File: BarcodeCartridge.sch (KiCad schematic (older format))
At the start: 3 parts, among them J1 Cartridge Connector, U1 W25Q128

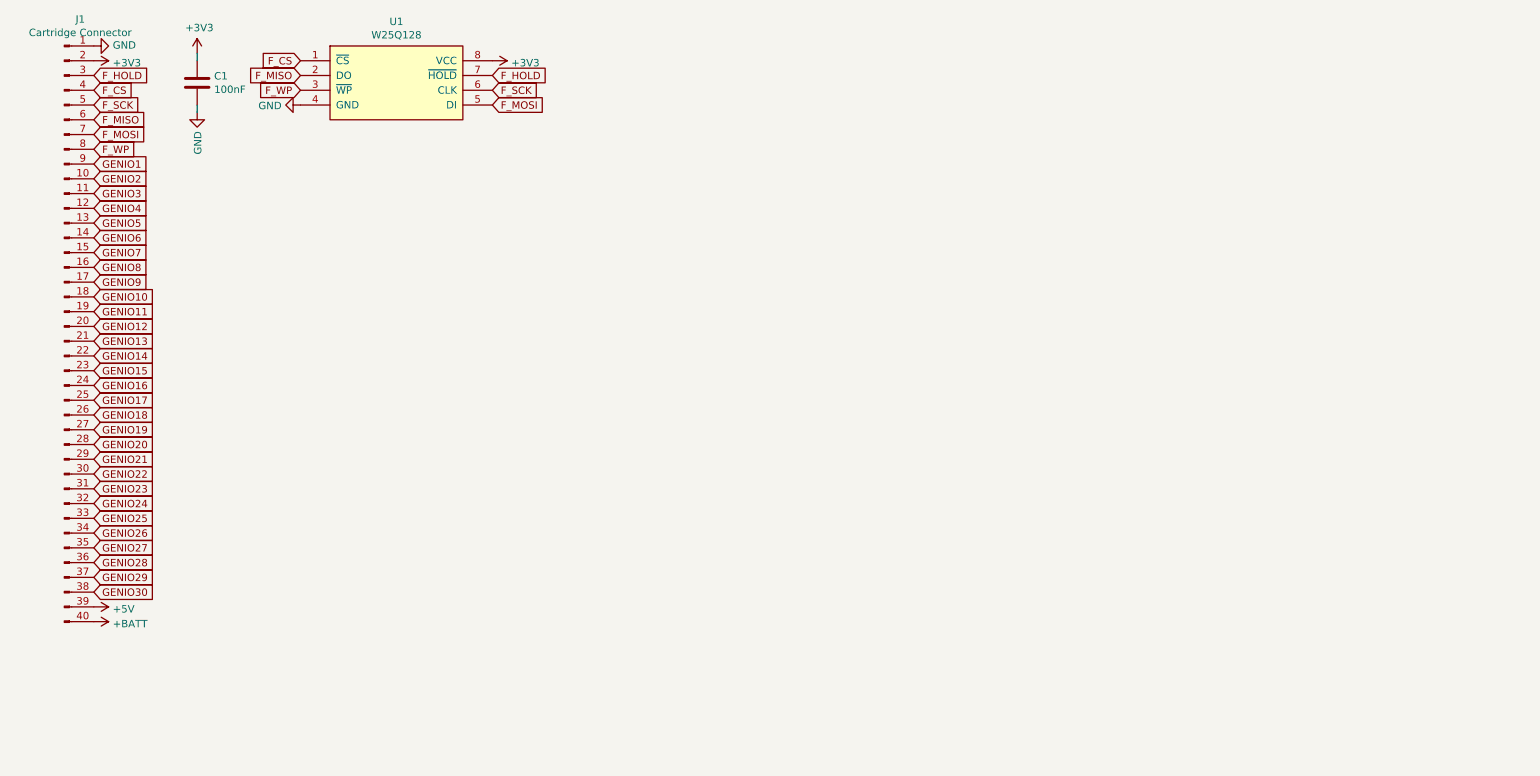
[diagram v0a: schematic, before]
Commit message: First design of the Barcode reader cartridge
Also updated:
- README
- Render image
- .gitignore
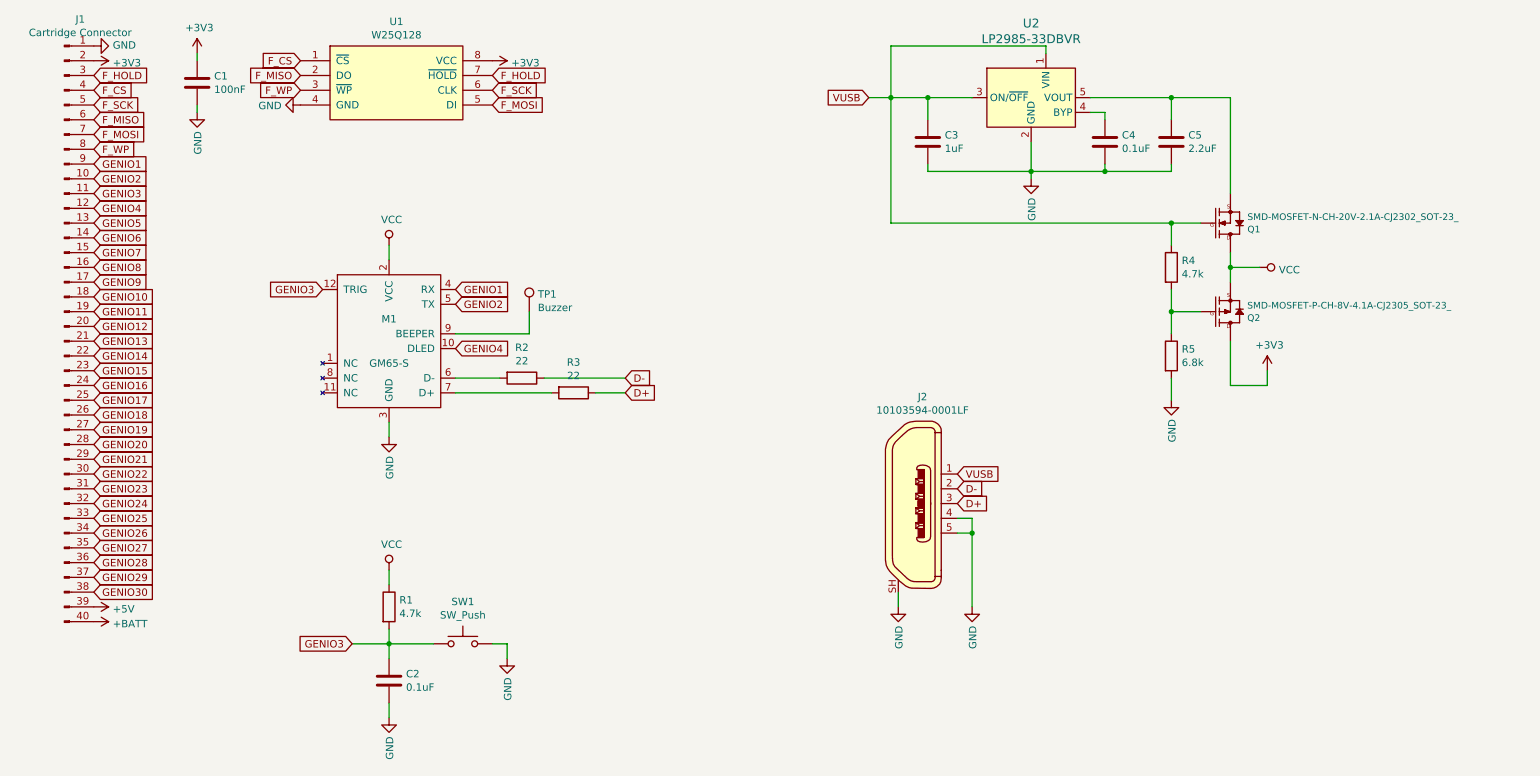
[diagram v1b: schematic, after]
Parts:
- added C2, C4: 0.1uF, Capacitors_SMD:C_0805_HandSoldering, symbol device:C
- added C3: 1uF, Capacitors_SMD:C_0805_HandSoldering, symbol device:C
- added C5: 2.2uF, Capacitors_SMD:C_0805_HandSoldering, symbol device:C
- added J2: 10103594-0001LF, digikey-footprints:USB_Micro_B_Female_10103594-0001LF, symbol dk_USB-DVI-HDMI-Connectors:10103594-0001LF
- added M1: GM65-S, SuperconCartridge:SD-52892-044, symbol SuperconCartridge:GM65-S
- added Q1: SMD-MOSFET-N-CH-20V-2.1A-CJ2302_SOT-23_, TO_SOT_Packages_SMD:SOT-23, symbol SeeedOPL-Transistor-2016:SMD-MOSFET-N-CH-20V-2.1A-CJ2302_SOT-23_
- added Q2: SMD-MOSFET-P-CH-8V-4.1A-CJ2305_SOT-23_, TO_SOT_Packages_SMD:SOT-23, symbol SeeedOPL-Transistor-2016:SMD-MOSFET-P-CH-8V-4.1A-CJ2305_SOT-23_
- added R1, R4: 4.7k, Resistors_SMD:R_0805_HandSoldering, symbol device:R
- added R2, R3: 22, Resistors_SMD:R_0805_HandSoldering, symbol device:R
- added R5: 6.8k, Resistors_SMD:R_0805_HandSoldering, symbol device:R
- added SW1: SW_Push, Buttons_Switches_SMD:SW_SPST_PTS645, symbol Switch:SW_Push
- added TP1: Buzzer, Connectors_TestPoints:Test_Point_Pad_d2.0mm, symbol Connector:TestPoint
- added U2: LP2985-33DBVR, digikey-footprints:SOT-753, symbol dk_PMIC-Voltage-Regulators-Linear:LP2985-33DBVR
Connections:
- net +3V3: now also Q2.3 (D)
- net GENIO1: now also M1.4 (RX)
- net GENIO2: now also M1.5 (TX)
- net GENIO3: now also C2.1, M1.12 (TRIG), R1.2, SW1.1
- net GENIO4: now also M1.10 (DLED)
- net GND: now also C2.2, C3.2, C4.2, C5.2, J2.4, J2.5, J2.SH, M1.3 (GND), R5.2, SW1.2, U2.2 (GND)
- new net: M1.6 (D-), R2.2
- new net: M1.7 (D+), R3.2
- new net: M1.9 (BEEPER), TP1.1
- new net: C4.1, U2.4 (BYP)
- new net: C5.1, Q1.2 (S), U2.5 (VOUT)
- new net: Q2.1 (G), R4.2, R5.1
- new net D+: J2.3, R3.1
- new net D-: J2.2, R2.1
- new net VCC: M1.2 (VCC), Q1.3 (D), Q2.2 (S), R1.1
- new net VUSB: C3.1, J2.1, Q1.1 (G), R4.1, U2.1 (VIN), U2.3 (ON/~OFF)
